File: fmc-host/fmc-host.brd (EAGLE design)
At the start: 76.5 x 69 mm, 321 parts, among them J1 SMA002, J10 ASP-134488-01, J2 SMA002, J3 SMA002, J4 SMA002, J5 SMA002, J6 ESHF-105-01-L-D-SM-K-TR, J7 12226-8250-00FR, J8 95278-101A16LF, J9 FMC_SINGLE_WIDTH_MODULE, Q1 SI1012R, Q2 SI1012R, U1 SN74LVC2G34DCKR, U10 DS90UB934-Q1, U11 DS90UB934-Q1, U12 DS91M040, U13 AD5766BCPZ-RL7, U14 MCP47FEB02A0-E/ST, U15 LM4132AMF-2.5/NOPBCT-ND, U16 AD7617BSTZ, U17 AD5142BCPZ10, U18 LTM4622A, U19 TPS62293DRV, U2 SN65LVDS9638DGN, U20 TPS7A49, U21 TPS7A49, U22 TPS7A30, U23 24AA64ST, U24 LTM8049_BGA, U3 FIN1032MTCX, U4 LTC2875_DFN, U5 ADCMP600, U6 ADCMP600, U7 DG1412E, U8 DG1412E, U9 DG1412E, X2 OE-LOGO_7X5, X3 OE-LOGO_7X5

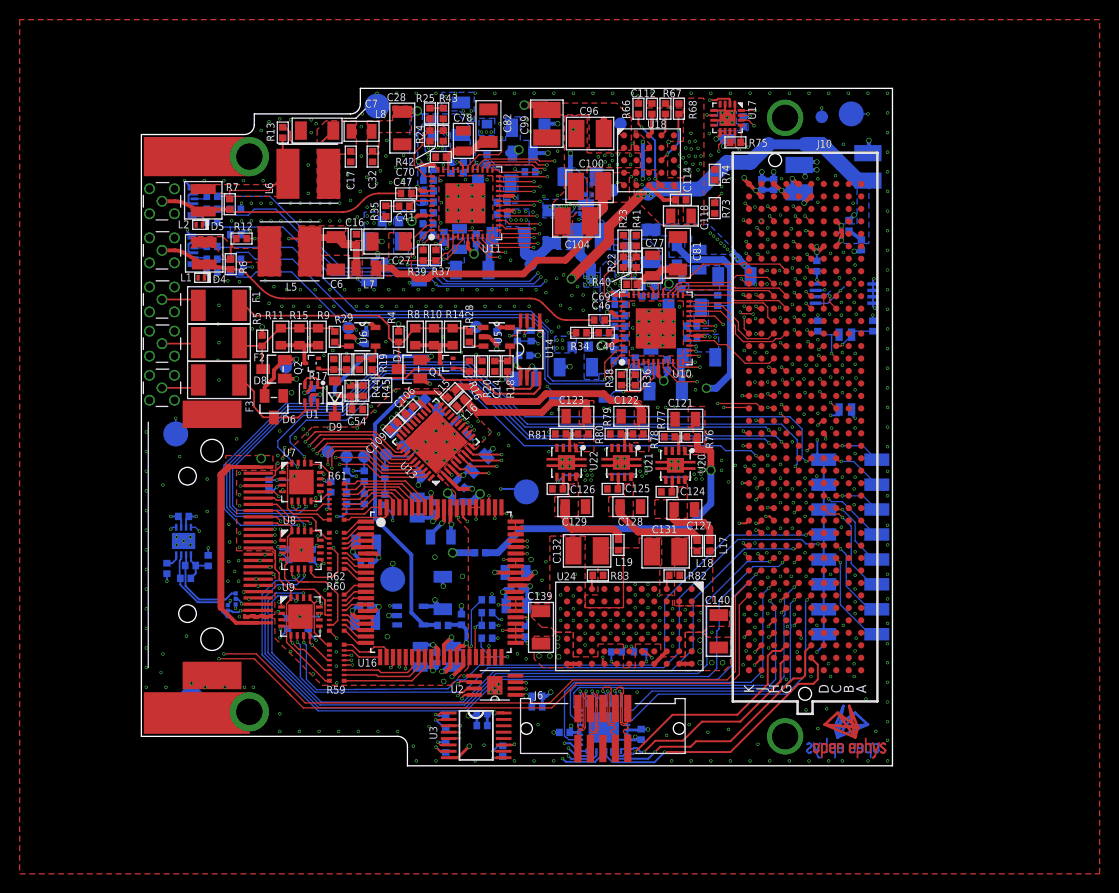
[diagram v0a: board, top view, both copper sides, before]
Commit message: ONIX FMC Host revision 1.5
- Lots of minor fixes after extensive testing of 1.4
- VITA-57 compliance
- Remove debug points
- Standalone 1.8V regulator for deserializers
- Lots of other small fixes
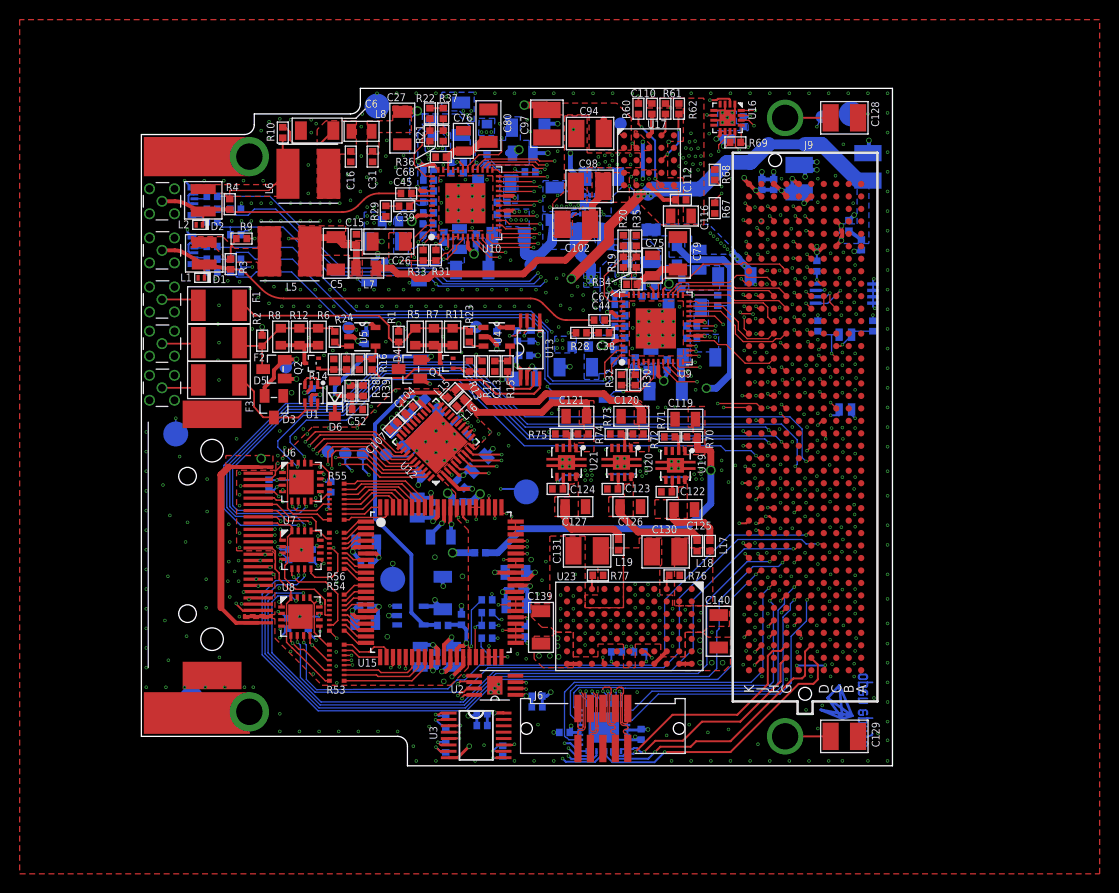
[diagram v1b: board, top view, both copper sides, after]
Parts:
- removed D10, D11: APFA3011-AK13/F, jonnew:RGB_LED_SMD-6
- removed D9: KDZ4.3B, jonnew:SOD123
- removed J10: ASP-134488-01, jonnew:FMC_HPC_MALE
- removed R82: 165k, jonnew:0402
- removed R83: 178k, jonnew:0402
- removed R84, R85: 10k, jonnew:0402
- removed R86, R87: 73.2k, jonnew:0402
- removed SJ1, SJ2: (no value), jonnew:SJ_2_0201
- removed U18: LTM4622A, jonnew:BGA_5X5_625X625
- removed X3: OE-LOGO_7X5, jonnew:OE-LOGO-7X5
- C100, C104, C132, C99: value 47uF -> 0.1uF; device jonnew:1210 -> jonnew:0402
- C101, C109, C113, C116, C117, C62, C69, C95: value 0.1uF -> 10uF; device jonnew:0402 -> jonnew:0805
- C102, C133: value 0.1uF -> 47uF; device jonnew:0402 -> jonnew:1210
- C106, C34, C70, C80, C91, C92: value 0.1uF -> 10uF; device jonnew:0402 -> jonnew:1206
- C107, C110, C111, C115, C61: value 10uF -> 0.1uF; device jonnew:0805 -> jonnew:0402
- C108, C120: device jonnew:1206 -> jonnew:0805
- C11, C20, C24, C50, C51, C57, C58: value 0.1uF -> 10nF
- C118, C71, C79: device jonnew:0805 -> jonnew:1206
- C122, C123: value 10uF -> 10nF; device jonnew:0805 -> jonnew:0402
- C125, C126, C59: value 10nF -> 10uF; device jonnew:0402 -> jonnew:0805
- C128, C129: value 10uF -> 0.1uF, 500V; device jonnew:0805 -> jonnew:1210
- C13, C22, C52, C53, C60, C84: value 10nF -> 0.1uF
- C26: value 10nF -> 10uF; device jonnew:0402 -> jonnew:1206
- C28: value 10uF -> 4.7nF; device jonnew:1206 -> jonnew:0402
- C30: value 4.7nF -> 0.1uF
- C38: value 10uF -> 47nF; device jonnew:1206 -> jonnew:0402
- C39: value 0.1uF -> 47nF
- C40: value 47nF -> 1uF; device jonnew:0402 -> jonnew:0805
- C41: value 47nF -> 0.1uF
- C44, C68, C78, C90: value 1uF -> 0.1uF; device jonnew:0805 -> jonnew:0402
- C5: value 4.7nF -> 10uF; device jonnew:0402 -> jonnew:1206
- C64: value 10uF -> 1uF
- C7, C83, C93: value 10uF -> 0.1uF; device jonnew:1206 -> jonnew:0402
- C74, C75: value 10uF -> 1uF; device jonnew:1206 -> jonnew:0805
- C77: value 1uF -> 10uF
- C82: value 10uF -> 10nF; device jonnew:1206 -> jonnew:0402
- C88: value 0.1uF -> 1uF; device jonnew:0402 -> jonnew:0805
- C94: value 10uF -> 47uF; device jonnew:1206 -> jonnew:1210
- C96: value 47uF -> 10uF; device jonnew:1210 -> jonnew:0805
- C97, C98: value 10uF -> 47uF; device jonnew:0805 -> jonnew:1210
- D1, D2: value HSMG-C280 -> SESD0402X1UN-0020-090; device jonnew:LED-0402 -> jonnew:0402P-DFN
- D3: value HSMG-C280 -> BAR66; device jonnew:LED-0402 -> jonnew:SOT23
- D4, D5: value SESD0402X1UN-0020-090 -> BAR66; device jonnew:0402P-DFN -> jonnew:SOT23
- D6: value BAR66 -> KDZ4.3B; device jonnew:SOT23 -> jonnew:SOD123
- D7, D8: value BAR66 -> APFA3011-AK13/F; device jonnew:SOT23 -> jonnew:RGB_LED_SMD-6
- J8: value 95278-101A16LF -> FMC_SINGLE_WIDTH_MODULE; device jonnew:JP2X8_SMD -> jonnew:FMC_SINGLE_WIDTH_MODULE
- J9: value FMC_SINGLE_WIDTH_MODULE -> ASP-134488-01; device jonnew:FMC_SINGLE_WIDTH_MODULE -> jonnew:FMC_HPC_MALE
- L13: value (none) -> 1277AS-H-6R8M=P2
- R1: value 2k -> 3k
- R10, R9: value 150,0.25W -> 2k; device jonnew:0603 -> jonnew:0402
- R12, R6, R7: value 2k -> 150,0.25W; device jonnew:0402 -> jonnew:0603
- R13: value 2k -> 165k
- R14: value 150,0.25W -> 165k; device jonnew:0603 -> jonnew:0402
- R15: value 150,0.25W -> 10k; device jonnew:0603 -> jonnew:0402
- R16: value 165k -> 10k
- R17: value 165k -> 1k
- R18, R41: value 10k -> 1k
- R19: value 10k -> 5.6k 1%
- R2, R38, R39: value 4.7k -> 3k
- R20: value 1k -> 21k 1%
- R21: value 1k -> 5.6k 1%
- R22: value 5.6k 1% -> 21k 1%
- R23: value 21k 1% -> 49.9
- R24: value 5.6k 1% -> 49.9
- R25: value 21k 1% -> 100
- R26, R27: value 60 1% -> 100
- R3: value 4.7k -> 2k
- R30, R31, R32: value 100 -> 4.7k
- R33: value 3k -> 4.7k
- R34: value 49.9 -> DNP
- R35: value 49.9 -> 10k
- R36: value 4.7k -> DNP
- R37, R79: value 4.7k -> 10k
- R4: value 3k -> 2k
- R40: value DNP -> 4.7k
- R42: value DNP -> 1k
- R43, R71, R73: value 10k -> 4.7k
- R44, R45: value 3k -> 1k
- R46: value 4.7k -> 1k
- R48: value 1k -> 0
- R49: value 4.7k -> 165k
- R5: value 3k -> 150,0.25W; device jonnew:0402 -> jonnew:0603
- R50, R51, R52: value 1k -> 165k
- R53: value 1k -> 2.2k; device jonnew:0402 -> jonnew:RN2X8-1506
- R54: value 0 -> 2.2k; device jonnew:0402 -> jonnew:RN2X8-1506
- R55, R56: value 165k -> 2.2k; device jonnew:0402 -> jonnew:RN2X8-1506
- R57, R58: value 165k -> 2k
- R59: value 2.2k -> 10k; device jonnew:RN2X8-1506 -> jonnew:0402
- R60, R61: value 2.2k -> 3.48k; device jonnew:RN2X8-1506 -> jonnew:0402
- R62: value 2.2k -> 649k; device jonnew:RN2X8-1506 -> jonnew:0402
- R63: value 2k -> 0
- R64: value 2k -> 10k
- R66, R67: value 3.48k -> 10k
- R68: value 649k -> 10k
- R69: value 0 -> 2.2k
- R70: value 10k -> 15k
- R72, R74: value 10k -> 47k
- R75: value 2.2k -> 4.7k
- R76: value 15k -> 165k
- R77: value 4.7k -> 178k
- R78: value 43k -> 10k
- R80: value 43k -> 73.2k
- R81: value 4.7k -> 73.2k
- U11: value DS90UB934-Q1 -> DS91M040; device jonnew:WQFN48-7X7-PAD -> jonnew:WQFN32-5X5
- U12: value DS91M040 -> AD5766BCPZ-RL7; device jonnew:WQFN32-5X5 -> jonnew:CP_40_7
- U13: value AD5766BCPZ-RL7 -> MCP47FEB02A0-E/ST; device jonnew:CP_40_7 -> jonnew:TSSOP-8
- U14: value MCP47FEB02A0-E/ST -> LM4132AMF-2.5/NOPBCT-ND; device jonnew:TSSOP-8 -> jonnew:SOT-23-5
- U15: value LM4132AMF-2.5/NOPBCT-ND -> AD7617BSTZ; device jonnew:SOT-23-5 -> jonnew:ST_80_2
- U16: value AD7617BSTZ -> AD5142BCPZ10; device jonnew:ST_80_2 -> jonnew:CP_16_27-L
- U17: value AD5142BCPZ10 -> LTM4622A; device jonnew:CP_16_27-L -> jonnew:BGA_5X5_625X625
- U19: value TPS62293DRV -> TPS7A49; device jonnew:WSON6-2X2 -> jonnew:PVSON-N8+4-3X3
- U21: value TPS7A49 -> TPS7A30
- U22: value TPS7A30 -> 24AA64ST; device jonnew:PVSON-N8+4-3X3 -> jonnew:TSSOP8
- U23: value 24AA64ST -> LTM8049_BGA; device jonnew:TSSOP8 -> jonnew:LTM8049
- U24: value LTM8049_BGA -> TPS62061DSGT; device jonnew:LTM8049 -> jonnew:WSON8-2X2
- U4: value LTC2875_DFN -> ADCMP600; device jonnew:DFN83X3 -> jonnew:SOT-23-5
- U6: value ADCMP600 -> DG1412E; device jonnew:SOT-23-5 -> jonnew:QFN16-4X4MM
- U9: value DG1412E -> DS90UB934-Q1; device jonnew:QFN16-4X4MM -> jonnew:WQFN48-7X7-PAD
- moved C82 63.9 mm to (-14.7, 0.20), flipped to the bottom, turned to 90 degrees
- moved C80 62.3 mm to (-30.2, 62.2), flipped to the top, turned to 270 degrees
- moved R25 62.1 mm to (-34.6, 1.40), flipped to the bottom, turned to 270 degrees
- moved C78 61.1 mm to (-22.5, 0.40), flipped to the bottom, turned to 180 degrees
- moved R60 59.8 mm to (-15.0, 63.9)
- moved C28 59.5 mm to (-25.3, 4.10), flipped to the bottom, turned to 180 degrees
- moved C32 58.5 mm to (-25.3, 3.00), flipped to the bottom, turned to 180 degrees
- moved R62 56.9 mm to (-10.8, 63.9)
- moved C115 56.2 mm to (-30.4, 11.3), turned to 180 degrees
- moved U16 55.6 mm to (-5.90, 63.0), turned to 270 degrees
- moved U11 55.2 mm to (-18.5, 0.90), flipped to the bottom
- moved C97 55.1 mm to (-24.3, 62.4), flipped to the top
- moved R66 53.6 mm to (-30.4, 12.6), flipped to the bottom, turned to 180 degrees
- moved R69 53.0 mm to (-5.10, 60.5), flipped to the top
- moved R61 52.2 mm to (-12.2, 63.9)
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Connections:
- removed net CAN_N: R27.2, SJ1.2, U4.6
- removed net CAN_P: R26.2, SJ2.2, U4.7
- removed net CAN_RX: J10.K8, U4.4
- removed net CAN_TX: J10.K7, U4.1
- removed net DEBUG0: J10.C10, J8.2
- removed net DEBUG1: J10.C11, J8.4
- removed net DEBUG2: J10.D14, J8.6
- removed net DEBUG3: J10.C14, J8.8
- removed net DEBUG4: J10.D15, J8.10
- removed net DEBUG5: J10.C15, J8.12
- removed net DEBUG6: J10.C18, J8.14
- removed net DEBUG7: J10.C19, J8.16
- removed net LVDS_DIN2_N/CAN_P: J7.2, SJ2.COM
- removed net LVDS_DIN2_P/CAN_N: J7.15, SJ1.COM
- removed net N$13: R33.2, U4.8
- removed net N$36: D3.C, R3.1
- removed net N$41: C5.1, R26.1, R27.1, U4.5
- removed net N$57: D1.A, R1.1
- removed net N$66: D2.A, R2.1
- new net FMC_PG: J9.D1, J9.F1
- new net N$51: C129.2, J9.CHASSIS_B
- new net N$52: C128.2, J9.CHASSIS_A
- net !ADC_CS: now also J9.H13, U15.63; no longer J10.H13, U16.63
- net !ADC_RESET: now also J9.F10, R66.2; no longer J10.F10, R72.2
- net !DAC_CS: now also J9.J16, U12.8; no longer J10.J16, U13.8
- net !DAC_RESET: now also J9.F14, U12.3; no longer J10.F14, U13.3
- net !LINK_PWR_ADJ_CS: now also J9.F38, U16.14; no longer J10.F38, U17.14
- net !LINK_PWR_ADJ_RESET: now also J9.E37, U16.16; no longer J10.E37, U17.16
- net $N1: now also D5.3, R12.2, R2.2, R24.1, R6.2, R8.2; no longer D8.3, R11.2, R15.2, R29.1, R5.2, R9.2
- net $N2: now also D3.3; no longer D6.3
- net $N3: now also D4.3, R1.2, R11.2, R23.1, R5.2, R7.2; no longer D7.3, R10.2, R14.2, R28.1, R4.2, R8.2
- net +12V: now also C116.2, C135.2, J9.C35, J9.C37, R38.2, R39.2, U17.A2, U17.B3, U17.D3, U17.E2; no longer C118.2, C130.2, J10.C35, J10.C37, R44.2, R45.2, U18.A2, U18.B3, U18.D3, U18.E2
- net +13V_AN: now also C104.2, C105.2, C7.2, U12.26, U6.11; no longer C10.2, C106.2, C107.2, R2.2, U13.26, U9.11
- net +15V: now also C130.2, R76.1, U23.A1, U23.A2, U23.B1, U23.B2; no longer C131.2, R82.1, U24.A1, U24.A2, U24.B1, U24.B2
- net +1V8: now also C106.2, C86.2, C87.2, C91.2, C92.2, R19.1, R21.1, R34.1, R36.1, U24.4, U9.17; no longer C108.2, C88.2, C89.2, C93.2, C94.2, R22.1, R24.1, R40.1, R42.1, U11.17, U19.3
- net +3V3: now also C10.2, C111.2, C114.2, C117.2, C118.2, C22.1, C28.1, C32.1, C74.2, C78.2, C82.2, C89.2, C93.2, C96.2, J9.E39, J9.F40, J9.G39, J9.H40, J9.J39, J9.K40, R30.2, R31.2, R32.2, R33.2, R40.2, R43.2, R57.2, R58.2, R63.1, R64.1, R65.1, R78.2, R79.2, U11.11, U11.12, U11.29, U11.30, U12.4, U13.1, U13.2, U15.49, U16.10, U16.15, U16.9, U23.A5, U23.A6, U23.A7, U23.B7, U23.K7, U23.L5, U23.L6, U23.L7, U24.5, U24.6, U24.7, U24.8, U4.5, U9.4, U9.5; no longer C11.2, C115.2, C116.2, C119.2, C120.2, C24.1, C30.1, C34.1, C39.1, C76.2, C80.2, C84.2, C91.2, C95.2, C98.2, J10.E39, J10.F40, J10.G39, J10.H40, J10.J39, J10.K40, R36.2, R37.2, R38.2, R39.2, R46.2, R49.2, R63.2, R64.2, R70.1, R71.1, R75.1, R84.2, R85.2, U11.4, U11.5, U12.11, U12.12, U12.29, U12.30, U13.4, U14.1, U14.2, U16.49, U17.10, U17.15, U17.9, U19.2, U19.4, U19.5, U24.A5, U24.A6, U24.A7, U24.B7, U24.K7, U24.L5, U24.L6, U24.L7, U4.3, U6.5
- net +5V_AN: now also C107.2, C108.2, C59.2, C62.2, C69.2, C77.2, C81.1, C83.2, C84.2, C90.2, U12.28, U14.3, U14.4, U15.15, U15.30, U15.6, U15.71; no longer C109.2, C110.2, C61.2, C64.2, C71.2, C79.2, C83.1, C86.2, C87.2, C92.2, R1.2, U13.28, U15.3, U15.4, U16.15, U16.30, U16.6, U16.71
- net -13V_AN: now also C103.2, C17.2, C99.2, U12.6, U12.PAD, U6.2, U6.PAD; no longer C101.2, C105.2, C20.2, R3.2, U13.6, U13.PAD, U9.2, U9.PAD
- net -15V: now also C131.1, R77.1, U23.G1, U23.G2, U23.H1, U23.H2, U23.J2; no longer C132.1, R83.1, U24.G1, U24.G2, U24.H1, U24.H2, U24.J2
- net ADC_BUSY: now also J9.J12, U15.67; no longer J10.J12, U16.67
- net ADC_CONVST: now also J9.K13, U15.68; no longer J10.K13, U16.68
- net ADC_MISO_A: now also J9.K11, U15.57; no longer J10.K11, U16.57
- net ADC_MISO_B: now also J9.J10, U15.56; no longer J10.J10, U16.56
- net ADC_MOSI: now also J9.K10, U15.55; no longer J10.K10, U16.55
- net ADC_SCLK: now also J9.J13, U15.62; no longer J10.J13, U16.62
- net ADDR0: now also J9.C27, R78.1; no longer J10.C27, R84.1
- net ADDR1: now also J9.C26, R79.1; no longer J10.C26, R85.1
- net AGND: now also C100.1, C104.1, C108.1, C17.1, C59.1, C62.1, C69.1, C7.1, C77.1, C81.2, C83.1, C84.1, C88.1, C95.1, C99.1, R48.1, R53.C2, R53.C4, R53.C6, R53.C7, R54.C1, R54.C3, R54.C5, R54.C6, R54.C7, R54.C8, R55.C2, R55.C3, R55.C5, R55.C7, R56.C1, R56.C2, R56.C3, R56.C4, R56.C6, R56.C8, U12.10, U12.20, U12.23, U12.24, U12.25, U12.29, U12.31, U14.2, U15.16, U15.29, U15.32, U15.34, U15.5, U15.69, U15.72, U6.3; no longer C10.1, C102.1, C106.1, C109.1, C110.1, C20.1, C61.1, C64.1, C71.1, C79.1, C83.2, C86.1, C87.1, C92.1, C97.1, D1.C, D2.C, D3.A, R54.1, R59.C2, R59.C4, R59.C6, R59.C7, R60.C1, R60.C3, R60.C5, R60.C6, R60.C7, R60.C8, R61.C2, R61.C3, R61.C5, R61.C7, R62.C1, R62.C2, R62.C3, R62.C4, R62.C6, R62.C8, U13.10, U13.20, U13.23, U13.24, U13.25, U13.29, U13.31, U15.2, U16.16, U16.29, U16.32, U16.34, U16.5, U16.69, U16.72, U9.3
- net AIN_AOUT0: now also J9.F11, U8.15; no longer J10.F11, U9.15
- net AIN_AOUT1: now also J9.D11, U8.6; no longer J10.D11, U9.6
- net AIN_AOUT10: now also J9.G19, U6.6; no longer J10.G19, U7.6
- net AIN_AOUT11: now also J9.H19, U6.15; no longer J10.H19, U7.15
- net AIN_AOUT2: now also J9.E12, U8.7; no longer J10.E12, U9.7
- net AIN_AOUT3: now also J9.H10, U8.14; no longer J10.H10, U9.14
- net AIN_AOUT4: now also J9.E18, U7.15; no longer J10.E18, U8.15
- net AIN_AOUT5: now also J9.J9, U7.6; no longer J10.J9, U8.6
- net AIN_AOUT6: now also J9.G10, U7.7; no longer J10.G10, U8.7
- net AIN_AOUT7: now also J9.F17, U7.14; no longer J10.F17, U8.14
- net AIN_AOUT8: now also J9.H20, U6.7; no longer J10.H20, U7.7
- net AIN_AOUT9: now also J9.J18, U6.14; no longer J10.J18, U7.14
- net AIO_0: now also R53.C1, U8.16; no longer R59.C1, U9.16
- net AIO_1: now also R53.C3, U8.5; no longer R59.C3, U9.5
- net AIO_10: now also R55.C4, U6.5; no longer R61.C4, U7.5
- net AIO_11: now also R55.C1, U6.16; no longer R61.C1, U7.16
- net AIO_2: now also R53.C5, U8.8; no longer R59.C5, U9.8
- net AIO_3: now also R53.C8, U8.13; no longer R59.C8, U9.13
- net AIO_4: now also R54.C4, U7.16; no longer R60.C4, U8.16
- net AIO_5: now also R54.C2, U7.5; no longer R60.C2, U8.5
- net AIO_6: now also R56.C5, U7.8; no longer R62.C5, U8.8
- net AIO_7: now also R56.C7, U7.13; no longer R62.C7, U8.13
- net AIO_8: now also R55.C6, U6.8; no longer R61.C6, U7.8
- net AIO_9: now also R55.C8, U6.13; no longer R61.C8, U7.13
- net AOUT0: now also U12.32, U6.1; no longer U13.32, U7.1
- net AOUT1: now also U12.33, U6.4; no longer U13.33, U7.4
- net AOUT10: now also U12.14, U8.4; no longer U13.14, U9.4
- net AOUT11: now also U12.15, U8.1; no longer U13.15, U9.1
- net AOUT2: now also U12.34, U6.9; no longer U13.34, U7.9
- net AOUT3: now also U12.35, U6.12; no longer U13.35, U7.12
- net AOUT4: now also U12.36, U7.1; no longer U13.36, U8.1
- net AOUT5: now also U12.37, U7.4; no longer U13.37, U8.4
- net AOUT6: now also U12.38, U7.12; no longer U13.38, U8.12
- net AOUT7: now also U12.39, U7.9; no longer U13.39, U8.9
- net AOUT8: now also U12.12, U8.9; no longer U13.12, U9.9
- net AOUT9: now also U12.13, U8.12; no longer U13.13, U9.12
- net CLKIN0: now also J9.D21, U4.1; no longer J10.D21, U5.1
- net CLKIN1: now also J9.E19, U5.1; no longer J10.E19, U6.1
- net CLKIN_TERM0: now also J9.K19, R17.1; no longer J10.K19, R20.1
- net CLKIN_TERM1: now also J9.K17, R18.1; no longer J10.K17, R21.1
- net CLKIN_VBIAS_SCL: now also J9.J21, R58.1, U13.7; no longer J10.J21, R64.1, U14.7
- net CLKIN_VBIAS_SDA: now also J9.K20, R57.1, U13.8; no longer J10.K20, R63.1, U14.8
- net CLKOUT: now also J9.D20; no longer J10.D20
- net DAC_MISO: now also J9.K16, U12.9; no longer J10.K16, U13.9
- net DAC_MOSI: now also J9.H14, U12.5; no longer J10.H14, U13.5
- net DAC_MUX: now also U12.27; no longer U13.27
- net DAC_SCLK: now also J9.J15, U12.7; no longer J10.J15, U13.7
- net DES_A_D0: now also J9.F34, U10.24; no longer J10.F34, U11.24
- net DES_A_D1: now also J9.K35, U10.23; no longer J10.K35, U11.23
- net DES_A_D10: now also J9.J31, U10.12; no longer J10.J31, U11.12
- net DES_A_D11: now also J9.K31, U10.11; no longer J10.K31, U11.11
- net DES_A_D2: now also J9.J34, U10.22; no longer J10.J34, U11.22
- net DES_A_D3: now also J9.K34, U10.21; no longer J10.K34, U11.21
- net DES_A_D4: now also J9.E33, U10.19; no longer J10.E33, U11.19
- net DES_A_D5: now also J9.J33, U10.18; no longer J10.J33, U11.18
- net DES_A_D6: now also J9.F32, U10.16; no longer J10.F32, U11.16
- net DES_A_D7: now also J9.E31, U10.15; no longer J10.E31, U11.15
- net DES_A_D8: now also J9.K32, U10.14; no longer J10.K32, U11.14
- net DES_A_D9: now also J9.F31, U10.13; no longer J10.F31, U11.13
- net DES_A_GPIO0: now also J9.J37, U10.28; no longer J10.J37, U11.28
- net DES_A_GPIO1: now also J9.K37, U10.27; no longer J10.K37, U11.27
- net DES_A_GPIO2: now also J9.J36, U10.26; no longer J10.J36, U11.26
- net DES_A_GPIO3: now also J9.E34, R43.1, U10.25; no longer J10.E34, R49.1, U11.25
- net DES_A_HSYNC: now also J9.E30, U10.10; no longer J10.E30, U11.10
- net DES_A_LEDG: now also J9.F28, R47.2; no longer J10.F28, R53.2
- net DES_A_LOCK: now also J9.E27, R42.2, R50.2, U10.48; no longer J10.E27, R48.2, R56.2, U11.48
- net DES_A_PASS: now also J9.J28, R45.2, R52.2, U10.47; no longer J10.J28, R51.2, R58.2, U11.47
- net DES_A_PCLK: now also J9.K28, U10.8; no longer J10.K28, U11.8
- net DES_A_PDB: now also J9.F35, U10.30; no longer J10.F35, U11.30
- net DES_A_SCL: now also J9.F29, R31.1, U10.2; no longer J10.F29, R37.1, U11.2
- net DES_A_SDA\: now also J9.E28, R33.1, U10.1; no longer J10.E28, R39.1, U11.1
- net DES_A_VSYNC: now also J9.J30, U10.9; no longer J10.J30, U11.9
- net DES_B_D0: now also J9.H29, U9.24; no longer J10.H29, U10.24
- net DES_B_D1: now also J9.H28, U9.23; no longer J10.H28, U10.23
- net DES_B_D10: now also J9.G24, U9.12; no longer J10.G24, U10.12
- net DES_B_D11: now also J9.D23, U9.11; no longer J10.D23, U10.11
- net DES_B_D2: now also J9.G28, U9.22; no longer J10.G28, U10.22
- net DES_B_D3: now also J9.G27, U9.21; no longer J10.G27, U10.21
- net DES_B_D4: now also J9.D27, U9.19; no longer J10.D27, U10.19
- net DES_B_D5: now also J9.D26, U9.18; no longer J10.D26, U10.18
- net DES_B_D6: now also J9.H26, U9.16; no longer J10.H26, U10.16
- net DES_B_D7: now also J9.G25, U9.15; no longer J10.G25, U10.15
- net DES_B_D8: now also J9.H25, U9.14; no longer J10.H25, U10.14
- net DES_B_D9: now also J9.D24, U9.13; no longer J10.D24, U10.13
- net DES_B_GPIO0: now also J9.H32, U9.28; no longer J10.H32, U10.28
- net DES_B_GPIO1: now also J9.G31, U9.27; no longer J10.G31, U10.27
- net DES_B_GPIO2: now also J9.H31, U9.26; no longer J10.H31, U10.26
- net DES_B_GPIO3: now also J9.G30, R40.1, U9.25; no longer J10.G30, R46.1, U10.25
- net DES_B_HSYNC\: now also J9.H23, U9.10; no longer J10.H23, U10.10
- net DES_B_LEDG: now also J9.G21, R46.2; no longer J10.G21, R52.2
- net DES_B_LOCK: now also J9.J22, R41.2, R49.2, U9.48; no longer J10.J22, R47.2, R55.2, U10.48
- net DES_B_PASS: now also J9.K22, R44.2, R51.2, U9.47; no longer J10.K22, R50.2, R57.2, U10.47
- net DES_B_PCLK: now also J9.C22, U9.8; no longer J10.C22, U10.8
- net DES_B_PDB: now also J9.G33, U9.30; no longer J10.G33, U10.30
- net DES_B_SCL: now also J9.G22, R30.1, U9.2; no longer J10.G22, R36.1, U10.2
- net DES_B_SDA: now also J9.H22, R32.1, U9.1; no longer J10.H22, R38.1, U10.1
- net DES_B_VSYNC: now also J9.K23, U9.9; no longer J10.K23, U10.9
- net DI_VBIAS0: now also R15.1, U13.3; no longer R18.1, U14.3
- net DI_VBIAS1: now also R16.1, U13.4; no longer R19.1, U14.4
- net DOUTP_F_A: now also C45.2, D2.C, R4.2; no longer C47.2, D5.C, R7.2
- net DOUTP_F_B: now also C44.2, D1.C, R3.2; no longer C46.2, D4.C, R6.2
- net GND: now also C10.1, C102.1, C106.1, C109.1, C110.1, C115.2, C117.1, C122.2, C123.2, C125.1, C126.1, C13.2, C131.2, C132.1, C20.1, C22.2, C24.1, C28.2, C34.1, C40.1, C41.1, C46.1, C47.1, C5.1, C61.1, C64.1, C71.1, C79.1, C86.1, C87.1, C92.1, C97.1, D1.A, D2.A, D3.1, D4.1, D5.1, D6.A, D7.3, D7.5, D7.6, D8.3, D8.5, D8.6, J9.A1, J9.A12, J9.A13, J9.A16, J9.A17, J9.A20, J9.A21, J9.A24, J9.A25, J9.A28, J9.A29, J9.A32, J9.A33, J9.A36, J9.A37, J9.A4, J9.A40, J9.A5, J9.A8, J9.A9, J9.B10, J9.B11, J9.B14, J9.B15, J9.B18, J9.B19, J9.B2, J9.B22, J9.B23, J9.B26, J9.B27, J9.B3, J9.B30, J9.B31, J9.B34, J9.B35, J9.B38, J9.B39, J9.B6, J9.B7, J9.C1, J9.C12, J9.C13, J9.C16, J9.C17, J9.C20, J9.C21, J9.C24, J9.C25, J9.C28, J9.C29, J9.C32, J9.C33, J9.C34, J9.C36, J9.C38, J9.C4, J9.C40, J9.C5, J9.C8, J9.C9, J9.D10, J9.D13, J9.D16, J9.D19, J9.D2, J9.D22, J9.D25, J9.D28, J9.D3, J9.D35, J9.D37, J9.D39, J9.D6, J9.D7, J9.E1, J9.E11, J9.E14, J9.E17, J9.E20, J9.E23, J9.E26, J9.E29, J9.E32, J9.E35, J9.E38, J9.E4, J9.E40, J9.E5, J9.E8, J9.F12, J9.F15, J9.F18, J9.F2, J9.F21, J9.F24, J9.F27, J9.F3, J9.F30, J9.F33, J9.F36, J9.F39, J9.F6, J9.F9, J9.G1, J9.G11, J9.G14, J9.G17, J9.G20, J9.G23, J9.G26, J9.G29, J9.G32, J9.G35, J9.G38, J9.G4, J9.G40, J9.G5, J9.G8, J9.H12, J9.H15, J9.H18, J9.H2, J9.H21, J9.H24, J9.H27, J9.H3, J9.H30, J9.H33, J9.H36, J9.H39, J9.H6, J9.H9, J9.J1, J9.J11, J9.J14, J9.J17, J9.J20, J9.J23, J9.J26, J9.J29, J9.J32, J9.J35, J9.J38, J9.J4, J9.J40, J9.J5, J9.J8, J9.K12, J9.K15, J9.K18, J9.K2, J9.K21, J9.K24, J9.K27, J9.K3, J9.K30, J9.K33, J9.K36, J9.K39, J9.K6, J9.K9, R1.1, R13.1, R14.1, R2.1, R20.2, R22.2, R28.2, R29.2, R37.2, R48.2, R49.1, R50.1, R51.1, R52.1, R62.2, R67.2, R71.1, R73.1, R75.1, R80.2, R81.2, U11.31, U12.2, U13.5, U13.6, U15.37, U15.38, U15.39, U15.41, U15.42, U15.43, U15.44, U15.46, U15.47, U15.48, U15.50, U15.51, U15.53, U15.54, U15.58, U15.59, U15.60, U15.61, U15.64, U15.65, U15.66, U16.1, U16.3, U16.5, U16.7, U16.PAD, U17.B5, U17.C1, U17.C2, U17.C5, U17.D5, U19.3, U19.4, U19.PAD1, U19.PAD2, U19.PAD3, U19.PAD4, U19.PAD5, U22.1, U22.2, U22.7, U23.A3, U23.A4, U23.B3, U23.B4, U23.B5, U23.B6, U23.C2, U23.C3, U23.C4, U23.C5, U23.C6, U23.D1, U23.D2, U23.D3, U23.D4, U23.D5, U23.D7, U23.E1, U23.E2, U23.E3, U23.E4, U23.E5, U23.F1, U23.F2, U23.F5, U23.F6, U23.F7, U23.G3, U23.G4, U23.G5, U23.H3, U23.H4, U23.H5, U23.J3, U23.J4, U23.J5, U23.J6, U23.K1, U23.K2, U23.K3, U23.K4, U23.K5, U23.K6, U23.L1, U23.L2, U23.L3, U23.L4, U24.1, U24.3, U24.PAD, U9.43, U9.44, U9.46, U9.PAD; no longer C100.1, C104.1, C108.1, C115.1, C117.2, C122.1, C123.1, C125.2, C126.2, C13.1, C131.1, C132.2, C17.2, C22.1, C24.2, C28.1, C34.2, C38.1, C39.2, C44.1, C45.1, C5.2, C59.1, C62.1, C69.1, C7.1, C77.1, C81.1, C84.1, C88.1, C95.1, C99.1, D10.3, D10.5, D10.6, D11.3, D11.5, D11.6, D4.A, D5.A, D6.1, D7.1, D8.1, D9.A, J10.A1, J10.A12, J10.A13, J10.A16, J10.A17, J10.A20, J10.A21, J10.A24, J10.A25, J10.A28, J10.A29, J10.A32, J10.A33, J10.A36, J10.A37, J10.A4, J10.A40, J10.A5, J10.A8, J10.A9, J10.B10, J10.B11, J10.B14, J10.B15, J10.B18, J10.B19, J10.B2, J10.B22, J10.B23, J10.B26, J10.B27, J10.B3, J10.B30, J10.B31, J10.B34, J10.B35, J10.B38, J10.B39, J10.B6, J10.B7, J10.C1, J10.C12, J10.C13, J10.C16, J10.C17, J10.C20, J10.C21, J10.C24, J10.C25, J10.C28, J10.C29, J10.C32, J10.C33, J10.C34, J10.C36, J10.C38, J10.C4, J10.C40, J10.C5, J10.C8, J10.C9, J10.D10, J10.D13, J10.D16, J10.D19, J10.D2, J10.D22, J10.D25, J10.D28, J10.D3, J10.D35, J10.D37, J10.D39, J10.D6, J10.D7, J10.E1, J10.E11, J10.E14, J10.E17, J10.E20, J10.E23, J10.E26, J10.E29, J10.E32, J10.E35, J10.E38, J10.E4, J10.E40, J10.E5, J10.E8, J10.F12, J10.F15, J10.F18, J10.F2, J10.F21, J10.F24, J10.F27, J10.F3, J10.F30, J10.F33, J10.F36, J10.F39, J10.F6, J10.F9, J10.G1, J10.G11, J10.G14, J10.G17, J10.G20, J10.G23, J10.G26, J10.G29, J10.G32, J10.G35, J10.G38, J10.G4, J10.G40, J10.G5, J10.G8, J10.H12, J10.H15, J10.H18, J10.H21, J10.H24, J10.H27, J10.H3, J10.H30, J10.H33, J10.H36, J10.H39, J10.H6, J10.H9, J10.J1, J10.J11, J10.J14, J10.J17, J10.J20, J10.J23, J10.J26, J10.J29, J10.J32, J10.J35, J10.J38, J10.J4, J10.J40, J10.J5, J10.J8, J10.K12, J10.K15, J10.K18, J10.K2, J10.K21, J10.K24, J10.K27, J10.K3, J10.K30, J10.K33, J10.K36, J10.K39, J10.K6, J10.K9, J8.1, J8.11, J8.13, J8.15, J8.3, J8.5, J8.7, J8.9, R16.1, R17.1, R23.2, R25.2, R33.1, R34.2, R4.1, R41.2, R43.2, R5.1, R54.2, R55.1, R56.1, R57.1, R58.1, R73.2, R74.2, R77.1, R79.1, R81.1, R86.2, R87.2, U11.43, U11.44, U11.46, U12.31, U12.PAD, U13.2, U14.5, U14.6, U16.37, U16.38, U16.39, U16.41, U16.42, U16.43, U16.44, U16.46, U16.47, U16.48, U16.50, U16.51, U16.53, U16.54, U16.58, U16.59, U16.60, U16.61, U16.64, U16.65, U16.66, U17.1, U17.3, U17.5, U17.7, U17.PAD, U18.B5, U18.C1, U18.C2, U18.C5, U18.D5, U19.6, U19.PAD, U22.PAD1, U22.PAD2, U22.PAD3, U22.PAD4, U22.PAD5, U23.1, U23.2, U23.3, U23.4, U23.7, U24.A3, U24.A4, U24.B3, U24.B4, U24.B5, U24.B6, U24.C2, U24.C3, U24.C4, U24.C5, U24.C6, U24.D1, U24.D2, U24.D3, U24.D4, U24.D5, U24.D7, U24.E1, U24.E2, U24.E3, U24.E4, U24.E5, U24.F1, U24.F2, U24.F5, U24.F6, U24.F7, U24.G3, U24.G4, U24.G5, U24.H3, U24.H4, U24.H5, U24.J3, U24.J4, U24.J5, U24.J6, U24.K1, U24.K2, U24.K3, U24.K4, U24.K5, U24.K6, U24.L1, U24.L2, U24.L3, U24.L4, U4.PAD, U6.2
- net LINK_A_PWR_EN: now also J9.H37, R68.1, U17.B2; no longer J10.H37, R74.1, U18.B2
- net LINK_B_PWR_EN: now also J9.K38, R67.1, U17.D2; no longer J10.K38, R73.1, U18.D2
- net LINK_PWR_ADJ_MISO: now also J9.F37, R69.2, U16.13; no longer J10.F37, R75.2, U17.13
- net LINK_PWR_ADJ_MOSI: now also J9.E36, U16.12; no longer J10.E36, U17.12
- net LINK_PWR_ADJ_SCLK: now also J9.H38, U16.11; no longer J10.H38, U17.11
- net LVDS_DIN0: now also J9.J2; no longer J10.J2
- net LVDS_DIN0_N: now also R25.1; no longer R30.1
- net LVDS_DIN0_P: now also R25.2; no longer R30.2
- net LVDS_DIN1: now also J9.H5; no longer J10.H5
- net LVDS_DIN1_N: now also R26.1; no longer R31.1
- net LVDS_DIN1_P: now also R26.2; no longer R31.2
- net LVDS_DIN2: now also J9.H4; no longer J10.H4
- net LVDS_DIN2_N: now also J7.2, R27.1; no longer R32.1, SJ2.1
- net LVDS_DIN2_P: now also J7.15, R27.2; no longer R32.2, SJ1.1
- net LVDS_DOUT0: now also J9.J3; no longer J10.J3
- net LVDS_DOUT1: now also J9.K4; no longer J10.K4
- net MLDVS_EN: now also J9.H8, U11.10; no longer J10.H8, U12.10
- net MLDVS_RO0: now also J9.G2, U11.1; no longer J10.G2, U12.1
- net MLDVS_RO1: now also J9.E3, U11.3; no longer J10.E3, U12.3
- net MLDVS_RO2: now also J9.G7, U11.5; no longer J10.G7, U12.5
- net MLDVS_RO3: now also J9.F4, U11.7; no longer J10.F4, U12.7
- net MLVDS_CLK_0_N: now also U11.24; no longer U12.24
- net MLVDS_CLK_0_P: now also U11.23; no longer U12.23
- net MLVDS_CLK_1_N: now also U11.22; no longer U12.22
- net MLVDS_CLK_1_P: now also U11.21; no longer U12.21
- net MLVDS_CLK_2_N: now also U11.20; no longer U12.20
- net MLVDS_CLK_2_P: now also U11.19; no longer U12.19
- net MLVDS_CLK_3_N: now also U11.18; no longer U12.18
- net MLVDS_CLK_3_P: now also U11.17; no longer U12.17
- net MLVDS_DE_!RE0: now also J9.F7, U11.25, U11.26; no longer J10.F7, U12.25, U12.26
- net MLVDS_DE_!RE1: now also J9.E7, U11.27, U11.28; no longer J10.E7, U12.27, U12.28
- net MLVDS_DE_!RE2: now also J9.H7, U11.13, U11.14; no longer J10.H7, U12.13, U12.14
- net MLVDS_DE_!RE3: now also J9.F8, U11.15, U11.16; no longer J10.F8, U12.15, U12.16
- net MLVDS_DI0: now also J9.G3, U11.2; no longer J10.G3, U12.2
- net MLVDS_DI1: now also J9.E2, U11.4; no longer J10.E2, U12.4
- net MLVDS_DI2: now also J9.G6, U11.6; no longer J10.G6, U12.6
- net MLVDS_DI3: now also J9.F5, U11.8; no longer J10.F5, U12.8
- net N$1: now also U24.2; no longer U19.1
- net N$10: now also R60.1, U17.E4; no longer R66.1, U18.E4
- net N$100: now also R34.2, R35.1, U9.35; no longer R40.2, R41.1, U10.35
- net N$118: now also D7.1, R41.1; no longer D10.1, R47.1
- net N$119: now also D7.2, R44.1; no longer D10.2, R50.1
- net N$12: now also C112.2, U17.E3; no longer C114.2, U18.E3
- net N$122: now also R60.2, U16.2; no longer R66.2, U17.2
- net N$123: now also R61.2, U16.6; no longer R67.2, U17.6
- net N$145: now also R62.1, U17.C4; no longer R68.1, U18.C4
- net N$15: now also C125.2, U19.5, U19.8; no longer C127.2, U20.5, U20.8
- net N$16: now also D8.4, R47.1; no longer D11.4, R53.1
- net N$17: now also R80.1, U23.E7; no longer R86.1, U24.E7
- net N$18: now also C13.1, R15.2, U4.4; no longer C14.1, R18.2, U5.4
- net N$19: now also R24.2, U5.3; no longer R29.2, U6.3
- net N$2: now also R11.1, R5.1, R7.1; no longer R10.1, R14.1, R8.1
- net N$20: now also C14.1, R16.2, U5.4; no longer C15.1, R19.2, U6.4
- net N$200: now also C56.2, C61.2, C66.2, C73.2, U10.29, U10.7; no longer C58.2, C63.2, C68.2, C75.2, U11.29, U11.7
- net N$21: now also R10.2, R4.1; no longer R13.2, R7.1
- net N$22: now also C16.1, C6.2, R10.1; no longer C17.1, C7.2, R13.1
- net N$23: now also R55.1, U15.79; no longer R61.1, U16.79
- net N$24: now also C15.1, C5.2, R9.1; no longer C16.1, C6.2, R12.1
- net N$25: now also R77.2, U23.J1; no longer R83.2, U24.J1
- net N$26: now also D7.4, R46.1; no longer D10.4, R52.1
- net N$27: now also C45.1, U10.41; no longer C47.1, U11.41
- net N$28: now also C39.1, U10.42; no longer C41.1, U11.42
- net N$29: now also R76.2, U23.C1; no longer R82.2, U24.C1
- net N$3: now also R23.2, U4.3; no longer R28.2, U5.3
- net N$30: now also C36.2, C42.2, C47.2, U10.3; no longer C37.2, C44.2, C49.2, U11.3
- net N$31: now also C37.2, C43.2, U10.20; no longer C38.2, C45.2, U11.20
- net N$32: now also C39.2, R29.1; no longer C41.2, R35.1
- net N$33: now also C122.1, U19.6; no longer C124.1, U20.6
- net N$34: now also R14.2, R18.2; no longer R17.2, R21.2
- net N$35: now also U23.E6, U23.H7; no longer U24.E6, U24.H7
- net N$37: now also R13.2, R17.2; no longer R16.2, R20.2
- net N$38: now also C44.1, U9.41; no longer C46.1, U10.41
- net N$39: now also R55.2, U15.80; no longer R61.2, U16.80
- net N$4: now also R3.1, R9.2; no longer R12.2, R6.1
- net N$40: now also R70.1, R71.2, U19.2; no longer R76.1, R77.2, U20.2
- net N$402: now also U10.6; no longer U11.6
- net N$403: now also R21.2, R22.1, U10.37; no longer R24.2, R25.1, U11.37
- net N$404: now also R36.2, R37.1, U10.35; no longer R42.2, R43.1, U11.35
- net N$42: now also C126.2, U20.5, U20.8; no longer C128.2, U21.5, U21.8
- net N$43: now also C123.1, U20.6; no longer C125.1, U21.6
- net N$45: now also C68.2, C76.2, C80.2, U10.34; no longer C70.2, C78.2, C82.2, U11.34
- net N$46: now also C115.1, R66.1, U15.36; no longer C117.1, R72.1, U16.36
- net N$47: now also C55.2, C60.2, C64.2, C71.2, U9.29, U9.7; no longer C57.2, C62.2, C66.2, C73.2, U10.29, U10.7
- net N$48: now also C34.2, C40.2, C46.2, U9.3; no longer C35.2, C42.2, C48.2, U10.3
- net N$49: now also C35.2, C41.2, U9.20; no longer C36.2, C43.2, U10.20
- net N$5: now also R61.1, U17.A4; no longer R67.1, U18.A4
- net N$50: now also C67.2, C75.2, C79.2, U9.34; no longer C69.2, C77.2, C81.2, U10.34
- net N$500: now also C119.2, R70.2, U19.1; no longer C121.2, R76.2, U20.1
- net N$501: now also C120.2, R72.2, U20.1; no longer C122.2, R78.2, U21.1
- net N$502: now also C121.2, R74.2, U21.1; no longer C123.2, R80.2, U22.1
- net N$506: now also C100.2, R59.1, U15.33; no longer C102.2, R65.1, U16.33
- net N$53: now also D8.1, R42.1; no longer D11.1, R48.1
- net N$54: now also D8.2, R45.1; no longer D11.2, R51.1
- net N$55: now also C38.1, U9.42; no longer C40.1, U10.42
- net N$56: now also R72.1, R73.2, U20.2; no longer R78.1, R79.2, U21.2
- net N$58: now also C127.2, U21.5, U21.8; no longer C129.2, U22.5, U22.8
- net N$59: now also C124.1, U21.6; no longer C126.1, U22.6
- net N$60: now also R74.1, R75.2, U21.2; no longer R80.1, R81.2, U22.2
- net N$603: now also U9.6; no longer U10.6
- net N$604: now also R19.2, R20.1, U9.37; no longer R22.2, R23.1, U10.37
- net N$61: now also R65.2, U15.45; no longer R71.2, U16.45
- net N$62: now also R53.1, U15.28; no longer R59.1, U16.28
- net N$63: now also R64.2, U15.40; no longer R70.2, U16.40
- net N$64: now also C95.2, U15.31; no longer C97.2, U16.31
- net N$65: now also R53.2, U15.27; no longer R59.2, U16.27
- net N$67: now also C109.2, U15.52; no longer C111.2, U16.52
- net N$68: now also R55.8, U15.73; no longer R61.8, U16.73
- net N$69: now also C101.2, U15.70; no longer C103.2, U16.70
- net N$7: now also R12.1, R6.1, R8.1; no longer R11.1, R15.1, R9.1
- net N$71: now also R63.2, U15.35; no longer R69.2, U16.35
- net N$72: now also R56.7, U15.2; no longer R62.7, U16.2
- net N$73: now also R56.1, U15.10; no longer R62.1, U16.10
- net N$74: now also R55.7, U15.74; no longer R61.7, U16.74
- net N$75: now also R55.6, U15.75; no longer R61.6, U16.75
- net N$76: now also R55.5, U15.76; no longer R61.5, U16.76
- net N$77: now also R55.4, U15.77; no longer R61.4, U16.77
- net N$78: now also R55.3, U15.78; no longer R61.3, U16.78
- net N$79: now also R53.3, U15.26; no longer R59.3, U16.26
- net N$8: now also C110.2, U17.A3; no longer C112.2, U18.A3
- net N$80: now also R53.4, U15.25; no longer R59.4, U16.25
- net N$81: now also R53.5, U15.24; no longer R59.5, U16.24
- net N$82: now also R53.6, U15.23; no longer R59.6, U16.23
- net N$83: now also R53.8, U15.22; no longer R59.8, U16.22
- net N$84: now also R53.7, U15.21; no longer R59.7, U16.21
- net N$85: now also R54.2, U15.19; no longer R60.2, U16.19
- net N$86: now also R54.1, U15.20; no longer R60.1, U16.20
- net N$87: now also R54.4, U15.17; no longer R60.4, U16.17
- net N$88: now also R54.3, U15.18; no longer R60.3, U16.18
- net N$89: now also R54.5, U15.14; no longer R60.5, U16.14
- net N$9: now also R81.1, U23.G7; no longer R87.1, U24.G7
- net N$90: now also R54.6, U15.13; no longer R60.6, U16.13
- net N$91: now also R54.7, U15.12; no longer R60.7, U16.12
- net N$92: now also R54.8, U15.11; no longer R60.8, U16.11
- net N$93: now also C38.2, R28.1; no longer C40.2, R34.1
- net N$94: now also R56.8, U15.1; no longer R62.8, U16.1
- net N$95: now also R56.5, U15.4; no longer R62.5, U16.4
- net N$96: now also R56.6, U15.3; no longer R62.6, U16.3
- net N$97: now also R56.4, U15.7; no longer R62.4, U16.7
- net N$98: now also R56.3, U15.8; no longer R62.3, U16.8
- net N$99: now also R56.2, U15.9; no longer R62.2, U16.9
- net SCL: now also J9.C30, U22.6; no longer J10.C30, U23.6
- net SDA: now also J9.C31, U22.5; no longer J10.C31, U23.5
- net TDI-TDO: now also J9.D30, J9.D31; no longer J10.D30, J10.D31
- net VAUX: now also C132.2, J9.D32, U22.8; no longer C135.2, J10.D32, U23.8
- net VDD_FPDX_A: now also C12.2, C21.2, C25.2, U10.31, U10.40; no longer C13.2, C22.2, C26.2, U11.31, U11.40
- net VDD_FPDX_B: now also C11.2, C20.2, C24.2, U9.31, U9.40; no longer C12.2, C21.2, C25.2, U10.31, U10.40
- net VDD_PX_A: now also C49.2, C54.2, C58.2, C65.2, C72.2, U10.36, U10.45; no longer C53.2, C56.2, C60.2, C67.2, C74.2, U11.36, U11.45
- net VDD_PX_B: now also C48.2, C53.2, C57.2, C63.2, C70.2, U9.36, U9.45; no longer C52.2, C55.2, C59.2, C65.2, C72.2, U10.36, U10.45
- net VLINK_A: now also C27.2, C31.1, C94.2, C97.2, U17.A1, U17.B1; no longer C28.2, C32.1, C96.2, C99.2, U18.A1, U18.B1
- net VLINK_B: now also C102.2, C26.2, C30.1, C98.2, U17.D1, U17.E1; no longer C100.2, C104.2, C27.2, C31.1, U18.D1, U18.E1
- net VREF: now also C88.2, R59.2, U12.22, U14.5; no longer C90.2, R65.2, U13.22, U15.5
- net V_PROTECT: now also C52.2, D3.2, D4.2, D5.2, D6.C, R38.1, R39.1; no longer C54.2, D6.2, D7.2, D8.2, D9.C, R44.1, R45.1
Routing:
- net CAN_RX: track 83.6 -> 0.00 mm, vias 2 -> 0
- net CAN_TX: track 83.1 -> 0.00 mm, vias 2 -> 0
- net GND: track 157.5 -> 132.8 mm, vias 675 -> 701
- net DEBUG2: track 10.8 -> 0.00 mm, vias 1 -> 0
- net CAN_P: track 10.1 -> 0.00 mm
- net DEBUG0: track 9.88 -> 0.00 mm, vias 1 -> 0
- net CAN_N: track 9.17 -> 0.00 mm
- net DEBUG1: track 8.69 -> 0.00 mm, vias 1 -> 0
- net DEBUG3: track 7.40 -> 0.00 mm, vias 1 -> 0
- net DEBUG4: track 7.03 -> 0.00 mm, vias 1 -> 0
- net AGND: track 61.6 -> 55.9 mm, vias 58 -> 56
- net DEBUG6: track 5.24 -> 0.00 mm, vias 1 -> 0
- net +1V8: track 17.8 -> 22.9 mm
- net DEBUG7: track 4.72 -> 0.00 mm, vias 1 -> 0
- net DEBUG5: track 4.71 -> 0.00 mm, vias 1 -> 0
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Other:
- board text added: "AUX IO"
- board text added: "CLK IO"
- board text added: "HS IO"
- board text added: "ONIX FMC Host"
- board text added: "Rev. 1.5 JPN 2020"
- board text removed: "0"
- board text removed: "1"
- board text removed: "2"
- board text removed: "3"
- board text removed: "4"
- board text removed: "5"
- board text removed: "6"
- board text removed: "7"
- board text removed: "DEBUG"
- board text removed: "Deserializer/IO Board"
- board text removed: "Rev. 1.5 JPN, MWL@MIT 2020"
- board text removed: "SIG"
